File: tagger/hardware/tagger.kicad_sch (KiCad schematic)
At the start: 34 parts, among them J4 SWD, J7 TETHER_DATA, J8 DISPLAY, J9 IO_CONN, Q1 Q_NMOS_GSD, SW24 BOOT0, SW26 NRST, U2 STM32F103RGTx, U4 ST3485EB, Y3 CG04874-8M

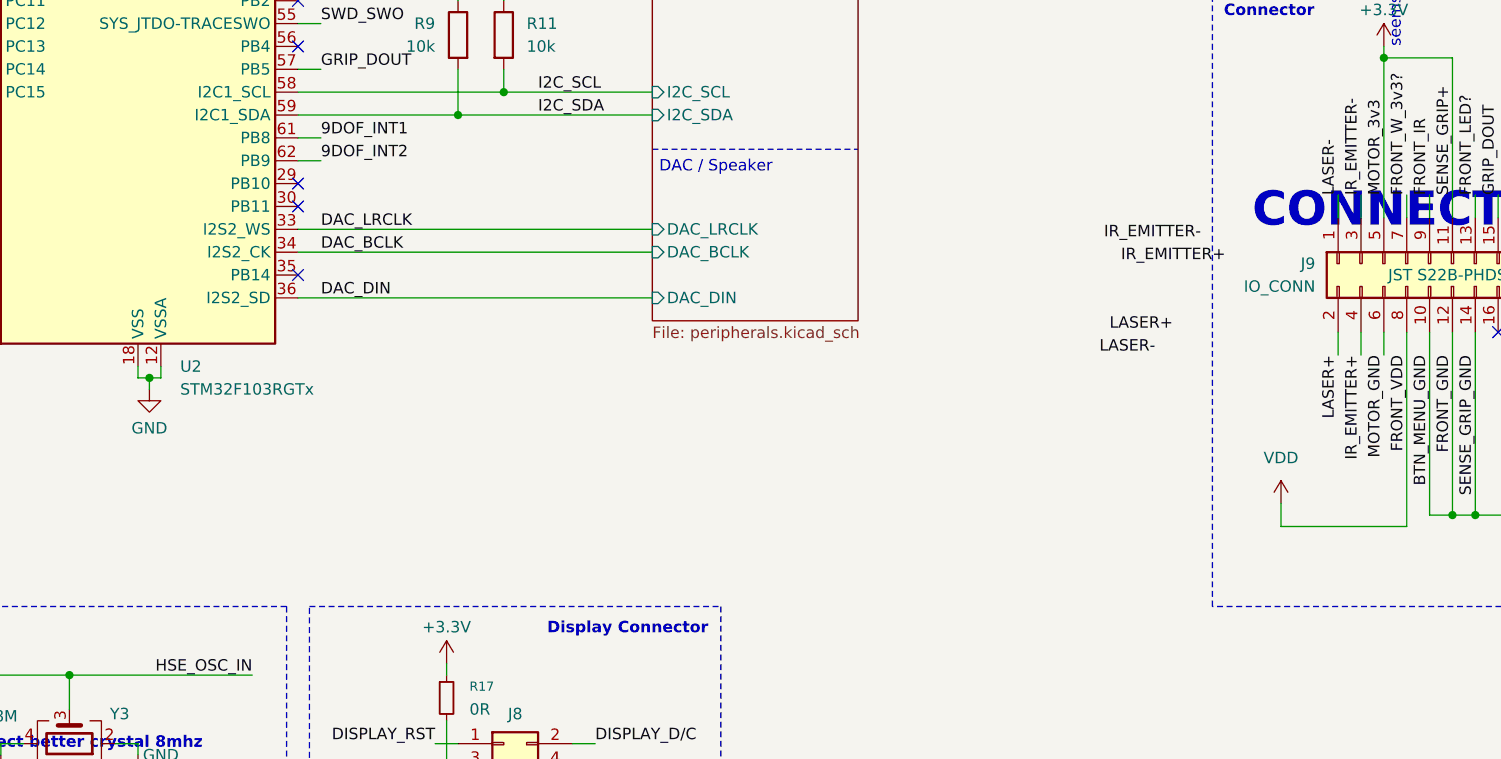
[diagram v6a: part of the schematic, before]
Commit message: feat: add IR routing, fix component sizes
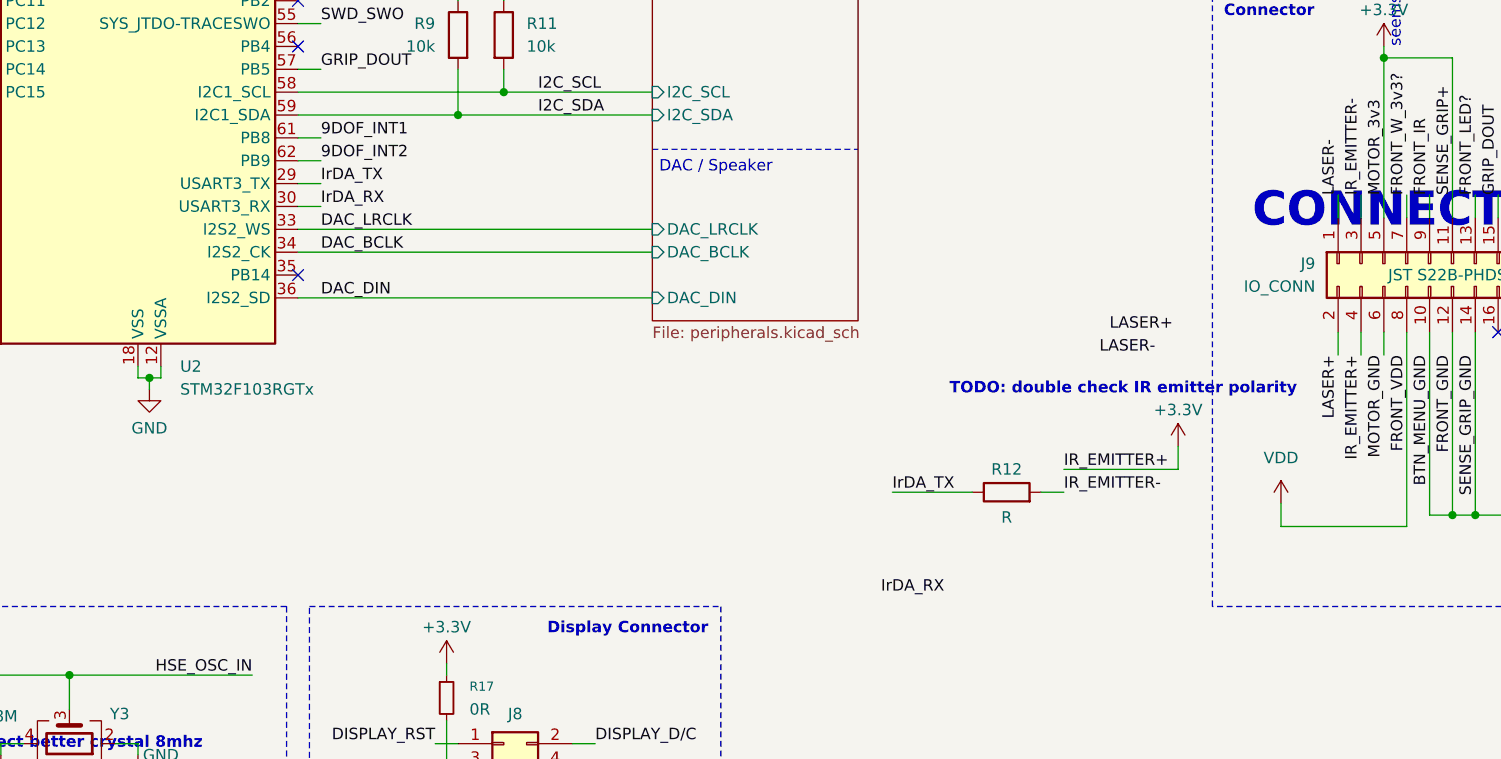
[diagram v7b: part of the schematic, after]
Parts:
- added R12: R, symbol Device:R
- C100, C101, C102, C103, C104, C4, C5, C66, C68, C7, C99: footprint Capacitor_SMD:C_0201_0603Metric_Pad0.64x0.40mm_HandSolder -> Capacitor_SMD:C_0402_1005Metric
- R11, R17, R19, R20, R21, R25, R26, R5, R9: footprint Resistor_SMD:R_0201_0603Metric_Pad0.64x0.40mm_HandSolder -> Resistor_SMD:R_0402_1005Metric
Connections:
- net IR_EMITTER+ is gone; now on net +3.3V: J9.4 (Pin_4)
- net IR_EMITTER-: now also R12.2
- net IrDA_TX: now reaches U2.29 (PB10)
- net IrDA_TX: now also R12.1
- net IrDA_RX: now reaches U2.30 (PB11)
- no-connect marks 13 -> 11
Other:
- note added: "TODO: double check IR emitter polarity"

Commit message: feat: added missing 3d models
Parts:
- J7: footprint Connector_PinHeader_2.00mm:PinHeader_1x02_P2.00mm_Horizontal -> tagger:S02B-PASK-2
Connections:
- net at R19.2, R21.1, TP1.1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: now also J7.2 (Pin_2); no longer J7.1 (Pin_1)
- net at R20.1, R21.2, TP2.1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: now also J7.1 (Pin_1); no longer J7.2 (Pin_2)
- no-connect marks 11 -> 20
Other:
- note added: "CHECK GREEN/YELLOW HOOKUPS"
- note added: "GREEN: YELLOW:"
- moved on the sheet: R11, R9
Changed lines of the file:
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@@
 		)
 	)
+	(text "GREEN:\nYELLOW:"
+		(exclude_from_sim no)
+		(at 278.638 26.162 0)
+		(effects
+			(font
+				(size 1.27 1.27)
+				(color 132 132 132 1)
+			)
+			(justify right top)
+		)
+	)
 	(text "HSE Crystal"
 		(exclude_from_sim no)
@@
 		)
 	)
+	(text "CHECK GREEN/YELLOW HOOKUPS"
+		(exclude_from_sim no)
+		(at 241.046 36.068 0)
+		(effects
+			(font
+				(size 3.81 3.81)
+				(thickness 0.762)
+				(bold yes)
+				(color 194 0 0 1)
+			)
+		)
+	)
 	(text "1x 100nf per VDD"
 		(exclude_from_sim no)
@@
 	)
 	(junction
-		(at 96.52 38.1)
+		(at 135.89 105.41)
 		(diameter 0)
 		(color 0 0 0 0)
 	)
 	(junction
-		(at 95.25 137.16)
+		(at 96.52 38.1)
 		(diameter 0)
 		(color 0 0 0 0)
 	)
 	(junction
-		(at 30.48 59.69)
+		(at 95.25 137.16)
 		(diameter 0)
 		(color 0 0 0 0)
 	)
 	(junction
-		(at 88.9 21.59)
+		(at 30.48 59.69)
 		(diameter 0)
 		(color 0 0 0 0)
 	)
 	(junction
-		(at 134.62 105.41)
+		(at 88.9 21.59)
 		(diameter 0)
 		(color 0 0 0 0)
@@
 	)
 	(junction
-		(at 132.08 92.71)
+		(at 41.91 31.75)
 		(diameter 0)
 		(color 0 0 0 0)
 	)
 	(junction
-		(at 41.91 31.75)
+		(at 232.41 101.6)
 		(diameter 0)
 		(color 0 0 0 0)
 	)
 	(junction
-		(at 232.41 101.6)
+		(at 64.77 185.42)
 		(diameter 0)
 		(color 0 0 0 0)
 	)
 	(junction
-		(at 64.77 185.42)
+		(at 128.27 107.95)
 		(diameter 0)
 		(color 0 0 0 0)
@@
 	)
 	(junction
+		(at 132.08 92.71)
+		(diameter 0)
+		(color 0 0 0 0)
+	)
+	(junction
 		(at 80.01 21.59)
 		(diameter 0)
@@
 	)
 	(junction
-		(at 129.54 107.95)
-		(diameter 0)
-		(color 0 0 0 0)
-	)
-	(junction
 		(at 93.98 38.1)
 		(diameter 0)
@@
 	)
 	(no_connect
+		(at 76.2 85.09)
+	)
+	(no_connect
 		(at 76.2 87.63)
 	)
@@
 	)
 	(no_connect
+		(at 76.2 92.71)
+	)
+	(no_connect
 		(at 76.2 62.23)
 	)
 	(no_connect
+		(at 76.2 82.55)
+	)
+	(no_connect
+		(at 111.76 85.09)
+	)
+	(no_connect
+		(at 76.2 77.47)
+	)
+	(no_connect
+		(at 76.2 97.79)
+	)
+	(no_connect
+		(at 76.2 95.25)
+	)
+	(no_connect
 		(at 245.11 132.08)
 	)
@@
 	)
 	(no_connect
+		(at 111.76 67.31)
+	)
+	(no_connect
 		(at 111.76 92.71)
 	)
@@
 	)
 	(no_connect
+		(at 76.2 80.01)
+	)
+	(no_connect
 		(at 142.24 182.88)
 	)
@@
 	(wire
 		(pts
+			(xy 132.08 92.71) (xy 135.89 92.71)
+		)
+		(stroke
+			(width 0)
+			(type default)
+		)
+	)
+	(wire
+		(pts
 			(xy 64.77 185.42) (xy 64.77 187.96)
 		)
@@
 	(wire
 		(pts
-			(xy 129.54 95.25) (xy 129.54 92.71)
+			(xy 128.27 95.25) (xy 128.27 92.71)
 		)
 		(stroke
@@
 	(wire
 		(pts
-			(xy 111.76 105.41) (xy 134.62 105.41)
+			(xy 111.76 105.41) (xy 135.89 105.41)
 		)
 		(stroke
@@
 	(wire
 		(pts
-			(xy 111.76 107.95) (xy 129.54 107.95)
+			(xy 111.76 107.95) (xy 128.27 107.95)
 		)
 		(stroke
@@
 	(wire
 		(pts
-			(xy 129.54 92.71) (xy 132.08 92.71)
+			(xy 128.27 92.71) (xy 132.08 92.71)
 		)
 		(stroke
@@
 		)
 	)
-	(wire
-		(pts
-			(xy 132.08 92.71) (xy 134.62 92.71)
-		)
-		(stroke
-			(width 0)
-			(type default)
-		)
-	)
 	(polyline
 		(pts
@@
 	(wire
 		(pts
+			(xy 128.27 107.95) (xy 151.13 107.95)
+		)
+		(stroke
+			(width 0)
+			(type default)
+		)
+	)
+	(wire
+		(pts
 			(xy 148.59 91.44) (xy 151.13 91.44)
 		)
@@
 	(wire
 		(pts
-			(xy 134.62 92.71) (xy 134.62 95.25)
+			(xy 135.89 92.71) (xy 135.89 95.25)
 		)
 		(stroke
@@
 	(wire
 		(pts
-			(xy 129.54 102.87) (xy 129.54 107.95)
+			(xy 128.27 102.87) (xy 128.27 107.95)
 		)
 		(stroke
@@
 	(wire
 		(pts
-			(xy 134.62 105.41) (xy 151.13 105.41)
-		)
-		(stroke
-			(width 0)
-			(type default)
-		)
-	)
-	(wire
-		(pts
 			(xy 111.76 52.07) (xy 114.3 52.07)
 		)
@@
 	(wire
 		(pts
-			(xy 134.62 102.87) (xy 134.62 105.41)
+			(xy 135.89 102.87) (xy 135.89 105.41)
 		)
 		(stroke
@@
 	(wire
 		(pts
+			(xy 135.89 105.41) (xy 151.13 105.41)
+		)
+		(stroke
+			(width 0)
+			(type default)
+		)
+	)
+	(wire
+		(pts
 			(xy 237.49 36.83) (xy 237.49 44.45)
 		)
@@
 	(wire
 		(pts
-			(xy 129.54 107.95) (xy 151.13 107.95)
-		)
-		(stroke
-			(width 0)
-			(type default)
-		)
-	)
-	(wire
-		(pts
 			(xy 111.76 54.61) (xy 114.3 54.61)
 		)
@@
 	(symbol
 		(lib_id "Device:R")
-		(at 129.54 99.06 0)
-		(mirror y)
+		(at 128.27 99.06 0)
 		(unit 1)
 		(exclude_from_sim no)
@@
 		(dnp no)
 		(property "Reference" "R9"
-			(at 127 97.7899 0)
+			(at 129.794 97.79 0)
 			(effects
 				(font
@@
 		)
 		(property "Value" "10k"
-			(at 127 100.3299 0)
+			(at 129.794 100.33 0)
 			(effects
 				(font
@@
 		)
 		(property "Footprint" "Resistor_SMD:R_0402_1005Metric"
-			(at 131.318 99.06 90)
+			(at 126.492 99.06 90)
 			(effects
 				(font
@@
 		)
 		(property "Datasheet" "~"
-			(at 129.54 99.06 0)
+			(at 128.27 99.06 0)
 			(effects
 				(font
@@
 		)
 		(property "Description" "Resistor"
-			(at 129.54 99.06 0)
+			(at 128.27 99.06 0)
 			(effects
 				(font
@@
 		)
 		(property "JLC" ""
-			(at 129.54 99.06 0)
+			(at 128.27 99.06 0)
 			(effects
 				(font
@@
 	(symbol
 		(lib_id "Device:R")
-		(at 134.62 99.06 0)
+		(at 135.89 99.06 0)
 		(unit 1)
 		(exclude_from_sim no)
@@
 		(on_board yes)
 		(dnp no)
-		(fields_autoplaced yes)
 		(property "Reference" "R11"
-			(at 137.16 97.7899 0)
+			(at 137.414 97.79 0)
 			(effects
 				(font
@@
 		)
 		(property "Value" "10k"
-			(at 137.16 100.3299 0)
+			(at 137.414 100.33 0)
 			(effects
 				(font
@@
 		)
 		(property "Footprint" "Resistor_SMD:R_0402_1005Metric"
-			(at 132.842 99.06 90)
+			(at 134.112 99.06 90)
 			(effects
 				(font
@@
 		)
 		(property "Datasheet" "~"
-			(at 134.62 99.06 0)
+			(at 135.89 99.06 0)
 			(effects
 				(font
@@
 		)
 		(property "Description" "Resistor"
-			(at 134.62 99.06 0)
+			(at 135.89 99.06 0)
 			(effects
 				(font
@@
 		)
 		(property "JLC" ""
-			(at 134.62 99.06 0)
+			(at 135.89 99.06 0)
 			(effects
 				(font
@@
 	(symbol
 		(lib_id "Connector:Conn_01x02_Socket")
-		(at 270.51 49.53 0)
+		(at 270.51 52.07 0)
+		(mirror x)
 		(unit 1)
 		(exclude_from_sim no)
@@
 		(dnp no)
 		(property "Reference" "J7"
-			(at 270.51 47.498 0)
+			(at 270.51 43.688 0)
 			(effects
 				(font
@@
 		)
 		(property "Value" "TETHER_DATA"
-			(at 270.51 54.102 0)
+			(at 270.51 46.228 0)
 			(effects
 				(font
@@
 			)
 		)
-		(property "Footprint" "Connector_PinHeader_2.00mm:PinHeader_1x02_P2.00mm_Horizontal"
-			(at 270.51 49.53 0)
+		(property "Footprint" "tagger:S02B-PASK-2"
+			(at 270.51 52.07 0)
 			(effects
 				(font
@@
 		)
 		(property "Datasheet" "~"
-			(at 270.51 49.53 0)
+			(at 270.51 52.07 0)
 			(effects
 				(font
@@
 		)
 		(property "Description" "Generic connector, single row, 01x02, script generated"
-			(at 270.51 49.53 0)
+			(at 270.51 52.07 0)
 			(effects
 				(font
@@
 		)
 		(property "Conn" "S02B-PASK-2"
-			(at 270.51 56.388 0)
+			(at 270.51 54.356 0)
 			(effects
 				(font
@@
 		)
 		(property "JLC" ""
-			(at 270.51 49.53 0)
+			(at 270.51 52.07 0)
 			(effects
 				(font
@@
 	)
 	(sheet
-		(at 1.27 -16.51)
+		(at 151.13 19.05)
 		(size 20.32 12.7)
 		(exclude_from_sim no)
@@
 		)
 		(property "Sheetname" "Power"
-			(at 1.27 -17.2216 0)
+			(at 151.13 18.3384 0)
 			(effects
 				(font
@@
 		)
 		(property "Sheetfile" "power.kicad_sch"
-			(at 1.27 -3.2254 0)
+			(at 151.13 32.3346 0)
 			(effects
 				(font
